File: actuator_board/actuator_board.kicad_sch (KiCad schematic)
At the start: 29 parts, among them J1 Conn_01x10_Socket, U1 113991054, U2 MCP4018T-103E/LTY, U3 TCA9548APWR, U4 MCP4018T-103E/LTY, U5 MCP4018T-103E/LTY, U6 MCP4018T-103E/LTY, U7 MCP4018T-103E/LTY

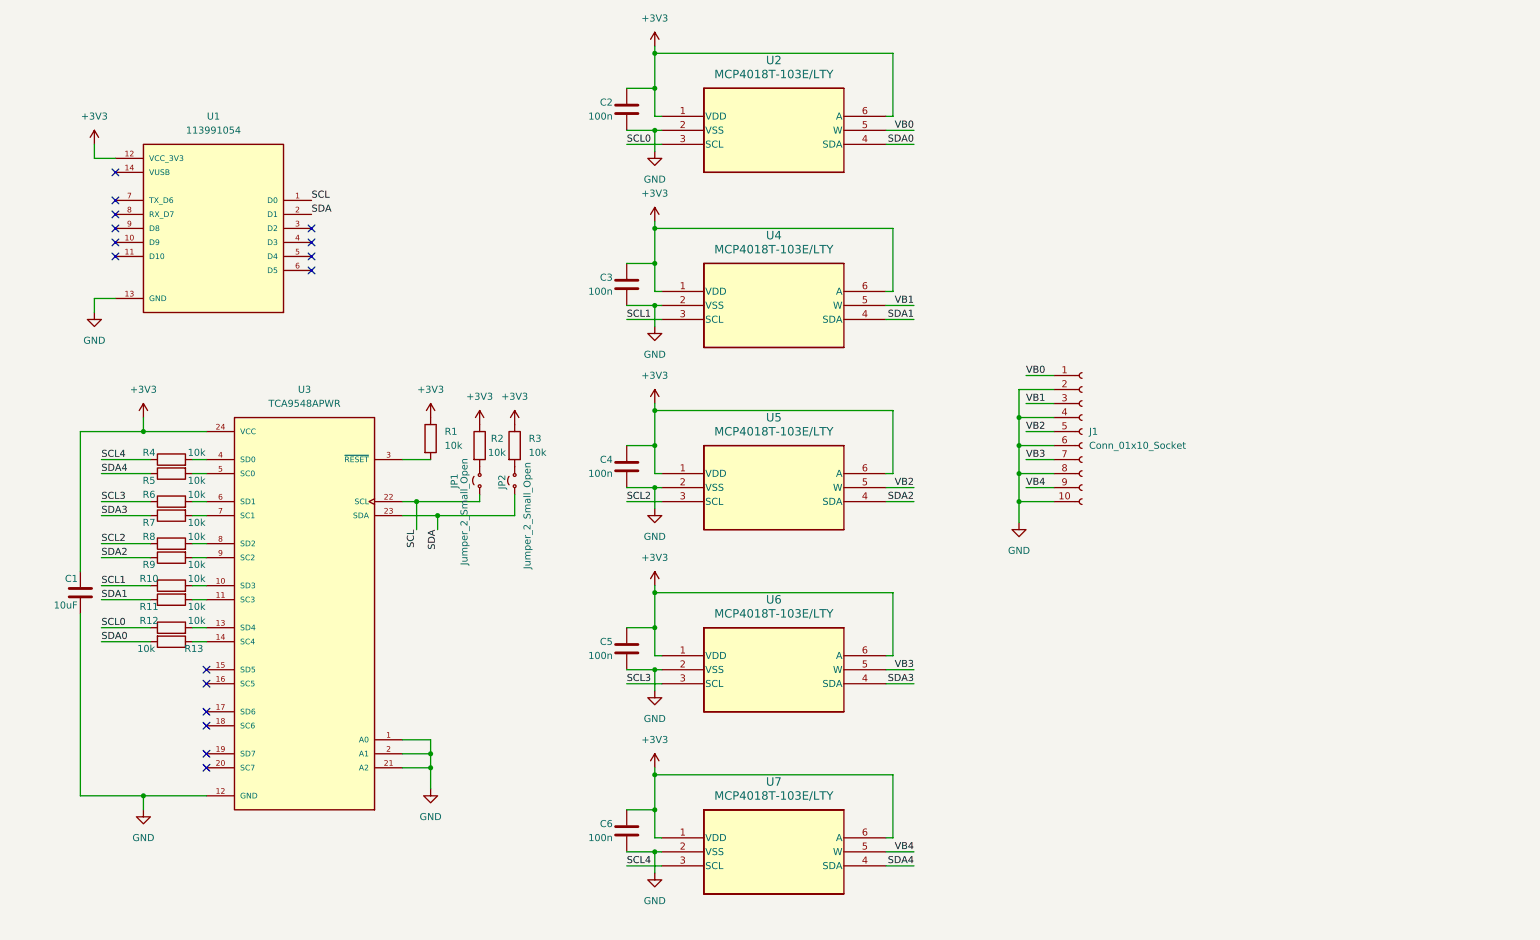
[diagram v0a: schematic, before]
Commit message: Actuator board schematic done
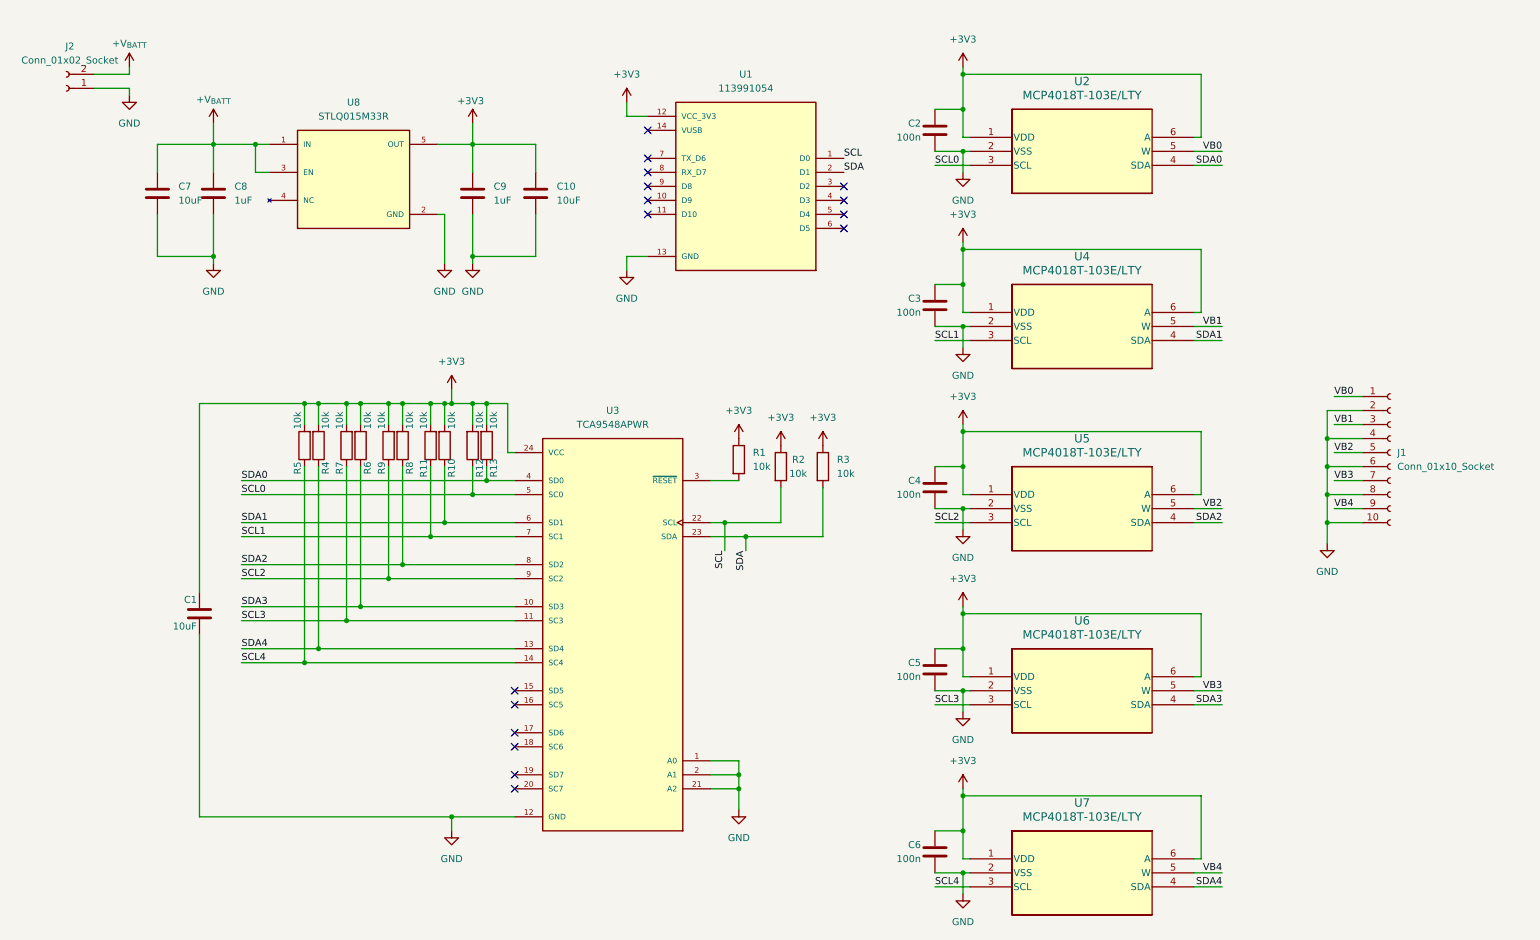
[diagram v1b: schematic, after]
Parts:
- removed JP1, JP2: Jumper_2_Small_Open, symbol Jumper:Jumper_2_Small_Open
- added C10, C7: 10uF, Capacitor_SMD:C_0805_2012Metric, symbol Device:C
- added C8, C9: 1uF, Capacitor_SMD:C_0805_2012Metric, symbol Device:C
- added J2: Conn_01x02_Socket, Connector_JST:JST_PH_B2B-PH-K_1x02_P2.00mm_Vertical, symbol Connector:Conn_01x02_Socket
- added U8: STLQ015M33R, STLQ015M33R:SOT95P280X145-5N, symbol STLQ015M33R:STLQ015M33R
- C1, C2, C3, C4, C5, C6: footprint (none) -> Capacitor_SMD:C_0805_2012Metric
- J1: footprint (none) -> Connector_PinSocket_1.00mm:PinSocket_1x10_P1.00mm_Vertical
- R1, R10, R11, R12, R13, R2, R3, R4, R5, R6, R7, R8, R9: footprint (none) -> Resistor_SMD:R_0805_2012Metric
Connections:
- net +3V3: now also R10.2, R11.2, R12.2, R13.2, R4.2, R5.2, R6.2, R7.2, R8.2, R9.2, C10.1, C9.1, U8.5 (OUT)
- net GND: now also C10.2, C7.2, C8.2, C9.2, J2.1 (Pin_1), U8.2 (GND)
- net SCL: now also R2.2
- net SCL0: now also U3.5 (SC0)
- net SCL1: now also R11.1, U3.7 (SC1); no longer R10.1
- net SCL2: now also R9.1, U3.9 (SC2); no longer R8.1
- net SCL3: now also R7.1, U3.11 (SC3); no longer R6.1
- net SCL4: now also R5.1, U3.14 (SC4); no longer R4.1
- net SDA: now also R3.2
- net SDA0: now also R13.1, U3.4 (SD0); no longer R13.2
- net SDA1: now also R10.1, U3.6 (SD1); no longer R11.1
- net SDA2: now also R8.1, U3.8 (SD2); no longer R9.1
- net SDA3: now also R6.1, U3.10 (SD3); no longer R7.1
- net SDA4: now also R4.1, U3.13 (SD4); no longer R5.1
- new net +V_{BATT}: C7.1, C8.1, J2.2 (Pin_2), U8.1 (IN), U8.3 (EN)
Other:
- moved on the sheet: C1, C2, C3, C4, C5, C6, J1, R1, R10, R11, R12, R13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

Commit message: Finished actuator board.
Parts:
- removed C1: 10uF, Capacitor_SMD:C_0805_2012Metric, symbol Device:C
- removed C2, C3, C4, C5, C6: 100n, Capacitor_SMD:C_0805_2012Metric, symbol Device:C
- removed R1, R10, R11, R12, R13, R2, R3, R4, R5, R6, R7, R8, R9: 10k, Resistor_SMD:R_0805_2012Metric, symbol Device:R
- removed U2, U4, U5, U6, U7: MCP4018T-103E/LTY, mcp4018:SC70-6_LT_MCH, symbol 2025-10-21_01-01-03:MCP4018T-103E_LTY
- removed U3: TCA9548APWR, TCA9548APWR:SOP65P640X120-24N, symbol TCA9548APWR:TCA9548APWR
- added D1, D2, D3, D4, D5: D_Schottky, PMEG2010EH_115:DIO_PMEG3020EH_115, symbol Device:D_Schottky
- added Q1, Q2, Q3, Q4, Q5: Q_NMOS_GSD, IRLML6344TRPBF:TRANS_IRLML6344TRPBF, symbol Transistor_FET:Q_NMOS_GSD
- added R1, R2, R3, R4, R5: 100R, Resistor_SMD:R_0805_2012Metric_Pad1.20x1.40mm_HandSolder, symbol Device:R_US
- added R10, R6, R7, R8, R9: 100k, Resistor_SMD:R_0805_2012Metric_Pad1.20x1.40mm_HandSolder, symbol Device:R_US
- C10, C7, C8, C9: footprint Capacitor_SMD:C_0805_2012Metric -> Capacitor_SMD:C_0805_2012Metric_Pad1.18x1.45mm_HandSolder
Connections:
- net VB0 is gone; now on net +V_{BATT}: J1.1 (Pin_1)
- net VB1 is gone; now on net +V_{BATT}: J1.3 (Pin_3)
- net VB2 is gone; now on net +V_{BATT}: J1.5 (Pin_5)
- net VB3 is gone; now on net +V_{BATT}: J1.7 (Pin_7)
- net VB4 is gone; now on net +V_{BATT}: J1.9 (Pin_9)
- net +V_{BATT}: now also D1.1 (K), D2.1 (K), D3.1 (K), D4.1 (K), D5.1 (K)
- net GND: now also Q1.2 (S), Q2.2 (S), Q3.2 (S), Q4.2 (S), Q5.2 (S), R10.2, R6.2, R7.2, R8.2, R9.2; no longer J1.10 (Pin_10), J1.2 (Pin_2), J1.4 (Pin_4), J1.6 (Pin_6), J1.8 (Pin_8)
- net at U1.3 (D2): now also R2.1
- net at U1.4 (D3): now also R3.1
- net at U1.5 (D4): now also R4.1
- net at U1.6 (D5): now also R5.1
- net SCL: no longer names the net of U1.1 (D0)
- net SDA: no longer names the net of U1.2 (D1)
- net SDA: now also R1.1
- new net MOTOR1-: D1.2 (A), J1.2 (Pin_2), Q1.3 (D)
- new net MOTOR2-: D2.2 (A), J1.4 (Pin_4), Q2.3 (D)
- new net MOTOR3-: D3.2 (A), J1.6 (Pin_6), Q3.3 (D)
- new net MOTOR4-: D4.2 (A), J1.8 (Pin_8), Q4.3 (D)
- new net MOTOR5-: D5.2 (A), J1.10 (Pin_10), Q5.3 (D)
- new net MOTORPWM1: Q1.1 (G), R1.2, R6.1
- new net MOTORPWM2: Q2.1 (G), R2.2, R7.1
- new net MOTORPWM3: Q3.1 (G), R3.2, R8.1
- new net MOTORPWM4: Q4.1 (G), R10.1, R4.2
- new net MOTORPWM5: Q5.1 (G), R5.2, R9.1
- no-connect marks 16 -> 7
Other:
- moved on the sheet: C10, C7, C8, C9, J1, J2, U1, U8

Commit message: Fixed actuator board and revised magnetometer board
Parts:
- J1: footprint Connector_PinSocket_1.00mm:PinSocket_1x10_P1.00mm_Vertical -> Connector_PinSocket_2.54mm:PinSocket_1x10_P2.54mm_Vertical
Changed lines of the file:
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@@
 			)
 		)
-		(property "Footprint" "Connector_PinSocket_1.00mm:PinSocket_1x10_P1.00mm_Vertical"
+		(property "Footprint" "Connector_PinSocket_2.54mm:PinSocket_1x10_P2.54mm_Vertical"
 			(at 264.16 110.49 0)
 			(effects

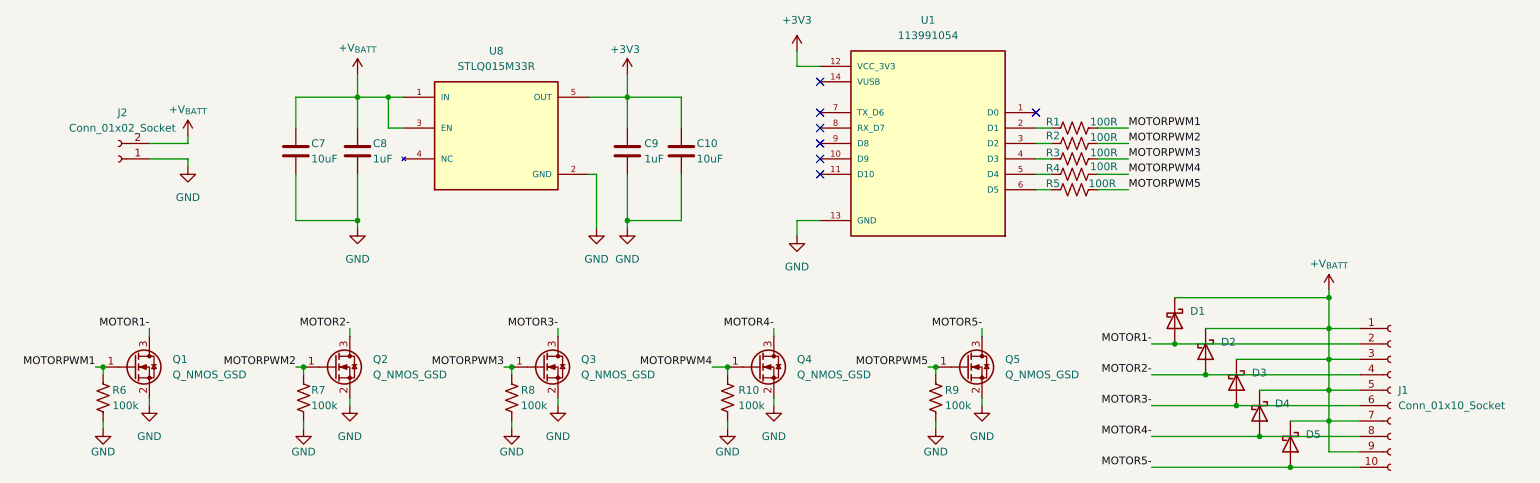
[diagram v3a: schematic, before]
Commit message: Fixed battery issues, removed LDOs
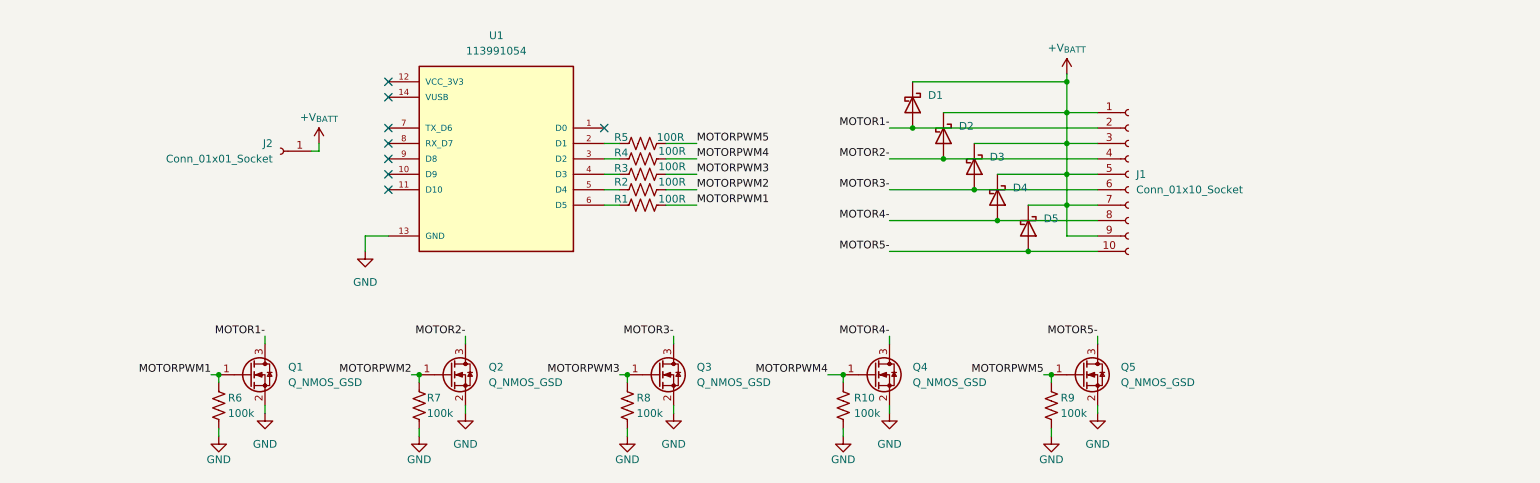
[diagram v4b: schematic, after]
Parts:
- removed C10, C7: 10uF, Capacitor_SMD:C_0805_2012Metric_Pad1.18x1.45mm_HandSolder, symbol Device:C
- removed C8, C9: 1uF, Capacitor_SMD:C_0805_2012Metric_Pad1.18x1.45mm_HandSolder, symbol Device:C
- removed J2: Conn_01x02_Socket, Connector_JST:JST_PH_B2B-PH-K_1x02_P2.00mm_Vertical, symbol Connector:Conn_01x02_Socket
- removed U8: STLQ015M33R, STLQ015M33R:SOT95P280X145-5N, symbol STLQ015M33R:STLQ015M33R
- added J2: Conn_01x01_Socket, Connector_PinSocket_2.54mm:PinSocket_1x01_P2.54mm_Vertical, symbol Connector:Conn_01x01_Socket
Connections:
- net +V_{BATT}: now also J2.1 (Pin_1)
- net at R2.1: now also U1.5 (D4); no longer U1.3 (D2)
- net at R4.1: now also U1.3 (D2); no longer U1.5 (D4)
- net at R1.1: now also U1.6 (D5); no longer U1.2 (D1)
- net at R5.1: now also U1.2 (D1); no longer U1.6 (D5)
- net +3V3: no longer names the net of U1.12 (VCC_3V3)
- no-connect marks 7 -> 8
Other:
- moved on the sheet: D1, D2, D3, D4, D5, J1, Q1, Q2, Q3, Q4, Q5, R1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
